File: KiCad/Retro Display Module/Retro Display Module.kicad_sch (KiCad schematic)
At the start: 51 parts, among them J10 Conn_01x02_Pin, J11 Conn_01x02_Pin, J12 VCC, J13 TX, J14 RX, J15 CFG, J16 SEL, J17 GND, J18 Conn_01x12_Pin, J2 VCC, J20 Conn_01x02_Pin, J21 Conn_01x04_Pin, J25 Conn_02x03_Odd_Even, J3 TX, J34 Conn_02x04_Odd_Even, J4 RX, J5 CFG, J6 SEL, J7 GND, J8 Conn_01x02_Pin, J9 Conn_01x02_Pin, U1 AO3401A, U2 AO3401A, U3 TS-1187A-B-A-B, U4 AO3401A, U5 STM32G030C8T6, U6 AO3401A, Y1 Crystal

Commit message: Begin STM32 Programming
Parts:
- H1, H2, H3, H4: now not fitted
- J10, J11, J20, J21, J8, J9: now left out of the parts list
- R1, R2, R3, R4, R7, R8, R9: footprint Library:R_0402_1005Metric -> Library:R_0402_1005Metric_Pad0.72x0.64mm_HandSolder
- R6: value 4.7k -> 100k; footprint Resistor_SMD:R_0805_2012Metric -> Library:R_0402_1005Metric_Pad0.72x0.64mm_HandSolder; LCSC C17673 -> C25741
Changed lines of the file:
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@@
       (effects (font (size 1.27 1.27)) (justify left))
     )
-    (property "Footprint" "Library:R_0402_1005Metric" (at 133.35 99.06 0)
+    (property "Footprint" "Library:R_0402_1005Metric_Pad0.72x0.64mm_HandSolder" (at 133.35 99.06 0)
       (effects (font (size 1.27 1.27)) hide)
     )
@@
       (effects (font (size 1.27 1.27)))
     )
-    (property "Footprint" "Library:R_0402_1005Metric" (at 24.13 113.03 0)
+    (property "Footprint" "Library:R_0402_1005Metric_Pad0.72x0.64mm_HandSolder" (at 24.13 113.03 0)
       (effects (font (size 1.27 1.27)) hide)
     )
@@
   )
   (symbol (lib_id "Connector:Conn_01x02_Pin") (at 205.74 137.16 0) (mirror x) (unit 1)
-    (in_bom yes) (on_board yes) (dnp yes)
+    (in_bom no) (on_board yes) (dnp yes)
     (property "Reference" "J20" (at 201.93 134.62 0)
       (effects (font (size 1.27 1.27)))
@@
   )
   (symbol (lib_id "Connector:Conn_01x04_Pin") (at 231.14 152.4 0) (mirror y) (unit 1)
-    (in_bom yes) (on_board yes) (dnp yes) (fields_autoplaced)
+    (in_bom no) (on_board yes) (dnp yes) (fields_autoplaced)
     (property "Reference" "J21" (at 231.8512 153.0263 0)
       (effects (font (size 1.27 1.27)) (justify right))
@@
   )
   (symbol (lib_id "Mechanical:MountingHole_Pad") (at 22.86 25.4 0) (unit 1)
-    (in_bom no) (on_board yes) (dnp no)
+    (in_bom no) (on_board yes) (dnp yes)
     (property "Reference" "H1" (at 21.59 17.78 0)
       (effects (font (size 1.27 1.27)) (justify left))
@@
   )
   (symbol (lib_id "Connector:Conn_01x02_Pin") (at 81.28 182.88 90) (unit 1)
-    (in_bom yes) (on_board yes) (dnp yes)
+    (in_bom no) (on_board yes) (dnp yes)
     (property "Reference" "J8" (at 87.63 184.15 90)
       (effects (font (size 1.27 1.27)))
@@
   )
   (symbol (lib_id "Connector:Conn_01x02_Pin") (at 88.9 19.05 90) (mirror x) (unit 1)
-    (in_bom yes) (on_board yes) (dnp yes)
+    (in_bom no) (on_board yes) (dnp yes)
     (property "Reference" "J9" (at 93.98 19.05 90)
       (effects (font (size 1.27 1.27)))
@@
     )
   )
+  (symbol (lib_id "Device:R_Small_US") (at 100.33 184.15 0) (unit 1)
+    (in_bom yes) (on_board yes) (dnp no)
+    (property "Reference" "R6" (at 96.52 185.42 0)
+      (effects (font (size 1.27 1.27)))
+    )
+    (property "Value" "100k" (at 96.52 182.88 0)
+      (effects (font (size 1.27 1.27)))
+    )
+    (property "Footprint" "Library:R_0402_1005Metric_Pad0.72x0.64mm_HandSolder" (at 100.33 184.15 0)
+      (effects (font (size 1.27 1.27)) hide)
+    )
+    (property "Datasheet" "~" (at 100.33 184.15 0)
+      (effects (font (size 1.27 1.27)) hide)
+    )
+    (property "LCSC" "C25741" (at 100.33 184.15 0)
+      (effects (font (size 1.27 1.27)) hide)
+    )
+    (pin "1")
+    (pin "2")
+    (instances
+      (project "Retro Display Module"
+        (path "/046eef48-6d3f-4288-a12a-fc20b7e12e30"
+          (reference "R6") (unit 1)
+        )
+        (path "/046eef48-6d3f-4288-a12a-fc20b7e12e30/d555fdcf-ac33-4f51-9933-2ad961069feb"
+          (reference "R31") (unit 1)
+        )
+      )
+    )
+  )
   (symbol (lib_id "Mechanical:MountingHole_Pad") (at 35.56 25.4 0) (unit 1)
-    (in_bom no) (on_board yes) (dnp no)
+    (in_bom no) (on_board yes) (dnp yes)
     (property "Reference" "H3" (at 34.29 17.78 0)
       (effects (font (size 1.27 1.27)) (justify left))
@@
       (effects (font (size 1.27 1.27)) (justify left))
     )
-    (property "Footprint" "Library:R_0402_1005Metric" (at 125.73 99.06 0)
+    (property "Footprint" "Library:R_0402_1005Metric_Pad0.72x0.64mm_HandSolder" (at 125.73 99.06 0)
       (effects (font (size 1.27 1.27)) hide)
     )
@@
   )
   (symbol (lib_id "Connector:Conn_01x02_Pin") (at 100.33 142.24 180) (unit 1)
-    (in_bom yes) (on_board yes) (dnp yes)
+    (in_bom no) (on_board yes) (dnp yes)
     (property "Reference" "J10" (at 107.95 138.43 0)
       (effects (font (size 1.27 1.27)))
@@
       (effects (font (size 1.27 1.27)))
     )
-    (property "Footprint" "Library:R_0402_1005Metric" (at 24.13 88.9 0)
+    (property "Footprint" "Library:R_0402_1005Metric_Pad0.72x0.64mm_HandSolder" (at 24.13 88.9 0)
       (effects (font (size 1.27 1.27)) hide)
     )
@@
         (path "/046eef48-6d3f-4288-a12a-fc20b7e12e30"
           (reference "J1") (unit 1)
-        )
-      )
-    )
-  )
-  (symbol (lib_id "Device:R_Small_US") (at 100.33 184.15 0) (unit 1)
-    (in_bom yes) (on_board yes) (dnp no) (fields_autoplaced)
-    (property "Reference" "R6" (at 101.981 183.5063 0)
-      (effects (font (size 1.27 1.27)) (justify left))
-    )
-    (property "Value" "4.7k" (at 101.981 185.4273 0)
-      (effects (font (size 1.27 1.27)) (justify left))
-    )
-    (property "Footprint" "Resistor_SMD:R_0805_2012Metric" (at 100.33 184.15 0)
-      (effects (font (size 1.27 1.27)) hide)
-    )
-    (property "Datasheet" "~" (at 100.33 184.15 0)
-      (effects (font (size 1.27 1.27)) hide)
-    )
-    (property "LCSC" "C17673" (at 100.33 184.15 0)
-      (effects (font (size 1.27 1.27)) hide)
-    )
-    (pin "1")
-    (pin "2")
-    (instances
-      (project "Retro Display Module"
-        (path "/046eef48-6d3f-4288-a12a-fc20b7e12e30"
-          (reference "R6") (unit 1)
         )
       )
@@
       (effects (font (size 1.27 1.27)))
     )
-    (property "Footprint" "Library:R_0402_1005Metric" (at 24.13 97.79 0)
+    (property "Footprint" "Library:R_0402_1005Metric_Pad0.72x0.64mm_HandSolder" (at 24.13 97.79 0)
       (effects (font (size 1.27 1.27)) hide)
     )
@@
   )
   (symbol (lib_id "Mechanical:MountingHole_Pad") (at 29.21 25.4 0) (unit 1)
-    (in_bom no) (on_board yes) (dnp no)
+    (in_bom no) (on_board yes) (dnp yes)
     (property "Reference" "H2" (at 27.94 17.78 0)
       (effects (font (size 1.27 1.27)) (justify left))
@@
       (effects (font (size 1.27 1.27)))
     )
-    (property "Footprint" "Library:R_0402_1005Metric" (at 24.13 121.92 0)
+    (property "Footprint" "Library:R_0402_1005Metric_Pad0.72x0.64mm_HandSolder" (at 24.13 121.92 0)
       (effects (font (size 1.27 1.27)) hide)
     )
@@
   )
   (symbol (lib_id "Connector:Conn_01x02_Pin") (at 125.73 49.53 180) (unit 1)
-    (in_bom yes) (on_board yes) (dnp yes)
+    (in_bom no) (on_board yes) (dnp yes)
     (property "Reference" "J11" (at 127 43.18 90)
       (effects (font (size 1.27 1.27)))
@@
       (effects (font (size 1.27 1.27)))
     )
-    (property "Footprint" "Library:R_0402_1005Metric" (at 146.05 86.36 0)
+    (property "Footprint" "Library:R_0402_1005Metric_Pad0.72x0.64mm_HandSolder" (at 146.05 86.36 0)
       (effects (font (size 1.27 1.27)) hide)
     )
@@
   )
   (symbol (lib_id "Mechanical:MountingHole_Pad") (at 41.91 25.4 0) (unit 1)
-    (in_bom no) (on_board yes) (dnp no)
+    (in_bom no) (on_board yes) (dnp yes)
     (property "Reference" "H4" (at 40.64 17.78 0)
       (effects (font (size 1.27 1.27)) (justify left))

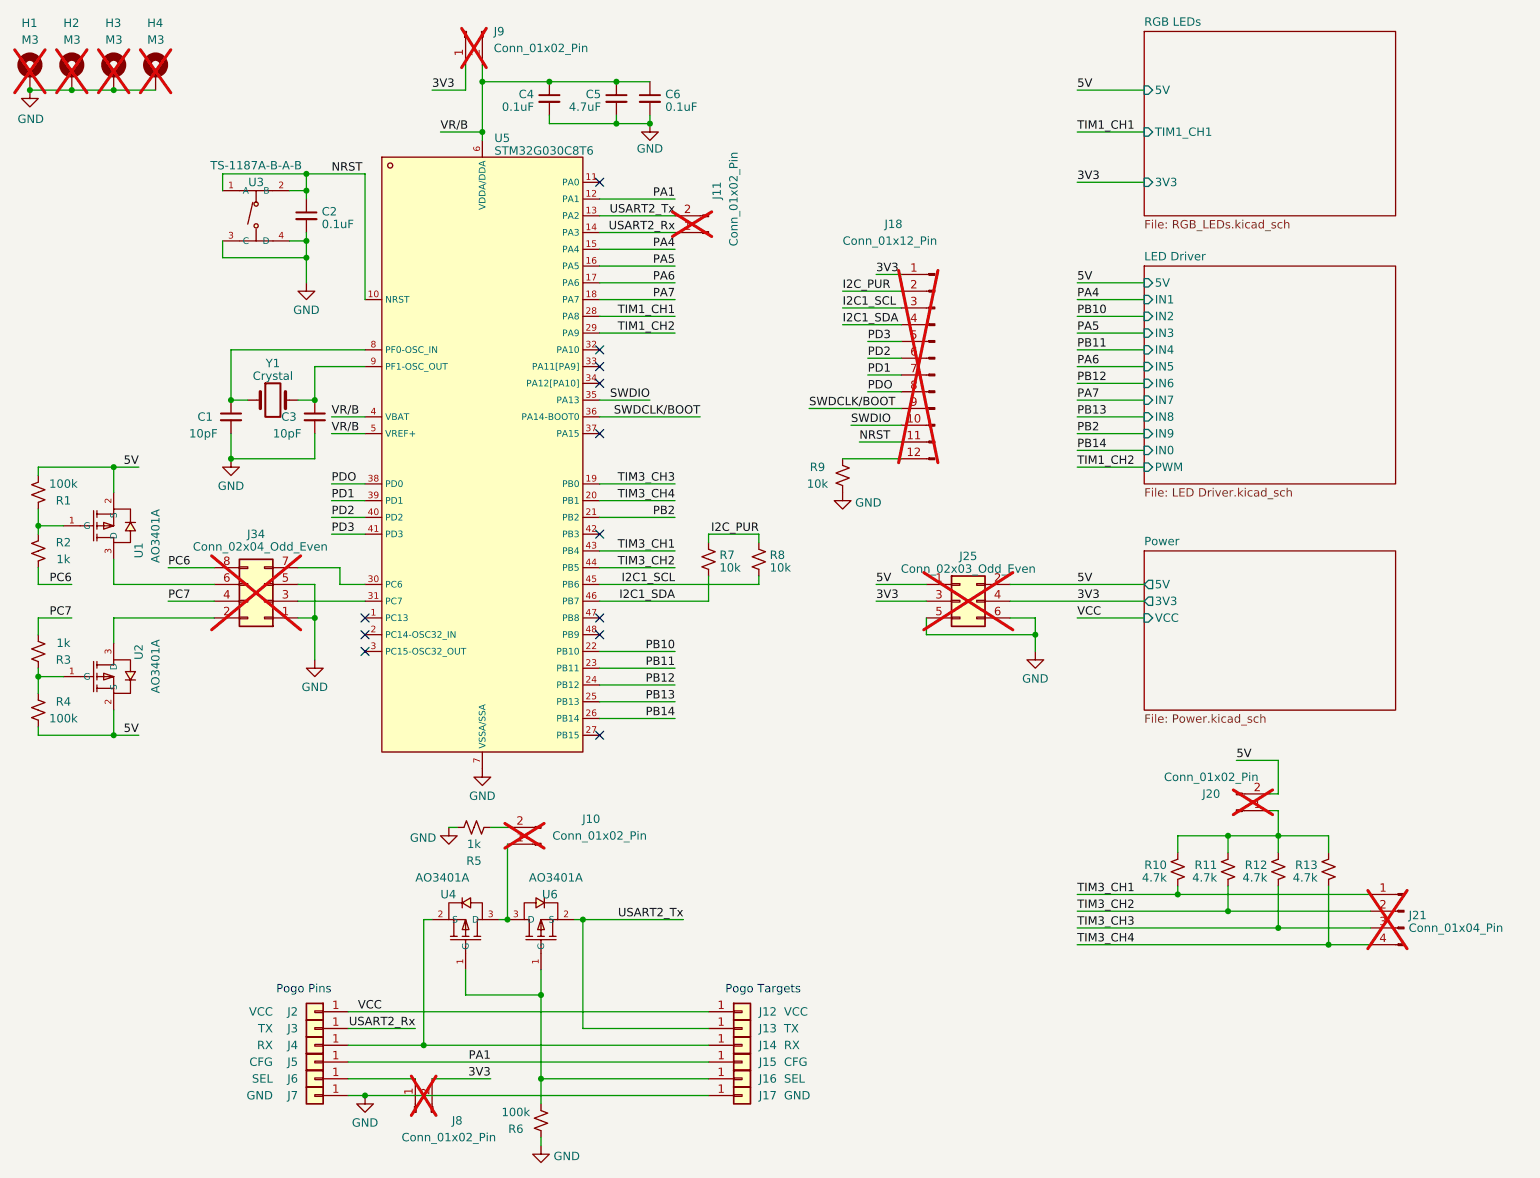
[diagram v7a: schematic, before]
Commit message: Updated Schematics and Added Reverse polarity protection
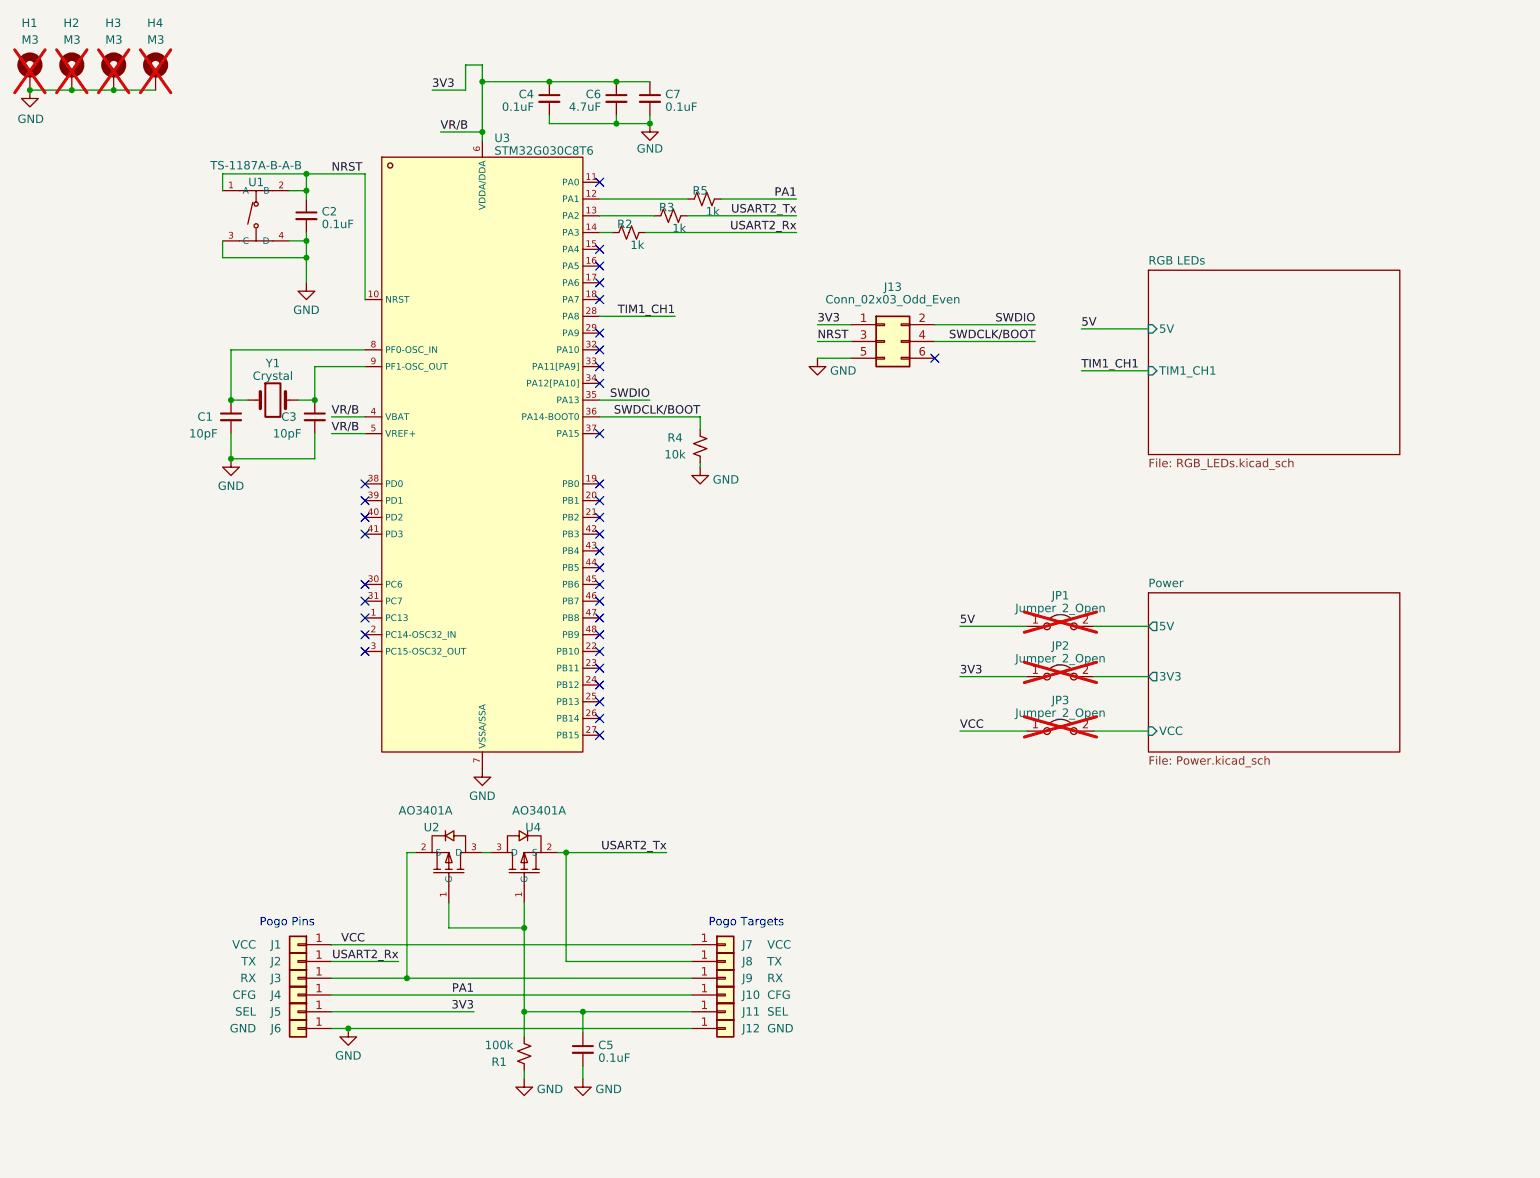
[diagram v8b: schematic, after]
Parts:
- removed J10, J11, J20, J8, J9: Conn_01x02_Pin, Connector_PinHeader_2.54mm:PinHeader_1x02_P2.54mm_Vertical, symbol Connector:Conn_01x02_Pin
- removed J18: Conn_01x12_Pin, Connector_PinHeader_2.54mm:PinHeader_1x12_P2.54mm_Vertical, symbol Connector:Conn_01x12_Pin
- removed J21: Conn_01x04_Pin, Connector_PinHeader_2.54mm:PinHeader_1x04_P2.54mm_Vertical, symbol Connector:Conn_01x04_Pin
- removed J25: Conn_02x03_Odd_Even, Connector_PinHeader_2.54mm:PinHeader_2x03_P2.54mm_Vertical, symbol Connector_Generic:Conn_02x03_Odd_Even
- removed J34: Conn_02x04_Odd_Even, Connector_PinHeader_2.54mm:PinHeader_2x04_P2.54mm_Vertical, symbol Connector_Generic:Conn_02x04_Odd_Even
- removed R1, R4: 100k, Library:R_0402_1005Metric_Pad0.72x0.64mm_HandSolder, symbol Device:R_Small_US
- removed R10, R11, R12, R13: 4.7k, Resistor_SMD:R_0805_2012Metric, symbol Device:R_Small_US
- removed R7, R8: 10k, Library:R_0402_1005Metric_Pad0.72x0.64mm_HandSolder, symbol Device:R_Small_US
- removed U1, U2: AO3401A, Library:SOT-23_L2.9-W1.3-P1.90-LS2.4-BR, symbol EEE4022S:AO3401A
- added C5: 0.1uF, Library:C_0402_1005Metric_Pad0.74x0.62mm_HandSolder, symbol Device:C_Small
- added J13: Conn_02x03_Odd_Even, Connector:Tag-Connect_TC2030-IDC-NL_2x03_P1.27mm_Vertical, symbol Connector_Generic:Conn_02x03_Odd_Even
- added JP1, JP2, JP3: Jumper_2_Open, Jumper:SolderJumper-2_P1.3mm_Open_RoundedPad1.0x1.5mm, symbol Jumper:Jumper_2_Open
- C1, C2, C3, C4: footprint Library:C_0402_1005Metric -> Library:C_0402_1005Metric_Pad0.74x0.62mm_HandSolder
- C6: renamed from C5; footprint Library:C_0402_1005Metric -> Library:C_0402_1005Metric_Pad0.74x0.62mm_HandSolder
- C7: renamed from C6; footprint Library:C_0402_1005Metric -> Library:C_0402_1005Metric_Pad0.74x0.62mm_HandSolder
- R5: footprint Resistor_SMD:R_0805_2012Metric -> Library:R_0402_1005Metric_Pad0.72x0.64mm_HandSolder; LCSC C17513 -> C11702
- renumbered J2 to J1, J15 to J10, J16 to J11, J17 to J12, J3 to J2, J4 to J3, J5 to J4, J6 to J5, J7 to J6, J12 to J7, J13 to J8, J14 to J9, R6 to R1, R9 to R4, U3 to U1, U4 to U2, U5 to U3, U6 to U4
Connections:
- net VR/B is gone; now on net 3V3: C4.1, C6.1, C7.1, U3.4 (VBAT), U3.5 (VREF+), U3.6 (VDDA/DDA)
- net 3V3: now also J5.1 (Pin_1), J13.1 (Pin_1), JP2.1 (A)
- net 5V: now also JP1.1 (A)
- net GND: now also C5.2, J13.5 (Pin_5); no longer R5.2
- net NRST: now also J13.3 (Pin_3)
- net PA1: now also R5.1; no longer U3.12 (PA1)
- net SWDCLK/BOOT: now also R4.2, J13.4 (Pin_4)
- net SWDIO: now also J13.2 (Pin_2)
- net USART2_Rx: now also R2.1; no longer U3.14 (PA3)
- net USART2_Tx: now also R3.1; no longer U3.13 (PA2)
- net VCC: now also JP3.1 (A)
- net at J11.1 (Pin_1), R1.1, U2.1 (G)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: now also C5.1
- net I2C1_SCL: no longer names the net of U3.45 (PB6)
- net I2C1_SDA: no longer names the net of U3.46 (PB7)
- net PA4: no longer names the net of U3.15 (PA4)
- net PA5: no longer names the net of U3.16 (PA5)
- net PA6: no longer names the net of U3.17 (PA6)
- net PA7: no longer names the net of U3.18 (PA7)
- net PB10: no longer names the net of U3.22 (PB10)
- net PB11: no longer names the net of U3.23 (PB11)
- net PB12: no longer names the net of U3.24 (PB12)
- net PB13: no longer names the net of U3.25 (PB13)
- net PB14: no longer names the net of U3.26 (PB14)
- net PB2: no longer names the net of U3.21 (PB2)
- net PC6: no longer names the net of R2.2
- net PC6: now also U3.14 (PA3)
- net PC7: no longer names the net of R3.2
- net PC7: now also U3.13 (PA2)
- net PD1: no longer names the net of U3.39 (PD1)
- net PD2: no longer names the net of U3.40 (PD2)
- net PD3: no longer names the net of U3.41 (PD3)
- net PDO: no longer names the net of U3.38 (PD0)
- net TIM1_CH2: no longer names the net of U3.29 (PA9)
- net TIM3_CH1: no longer names the net of U3.43 (PB4)
- net TIM3_CH2: no longer names the net of U3.44 (PB5)
- net TIM3_CH3: no longer names the net of U3.19 (PB0)
- net TIM3_CH4: no longer names the net of U3.20 (PB1)
- new net: R5.2, U3.12 (PA1)
- new net Power/3V3: JP2.2 (B)
- new net Power/5V: JP1.2 (B)
- new net Power/VCC: JP3.2 (B)
- no-connect marks 12 -> 36
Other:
- removed sheet LED Driver
- sheet RGB LEDs ports: added none; removed 3V3
- moved on the sheet: J1, J10, J11, J12, J2, J3, J4, J5, J6, J7, J8, J9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
